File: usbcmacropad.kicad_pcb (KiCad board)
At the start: 2 copper layers, 81 x 45.2 mm, 6 parts, among them SW1 SW_Push, SW2 SW_Push, SW3 SW_Push, SW4 SW_Push, U1 XIAO-RP2040-DIP

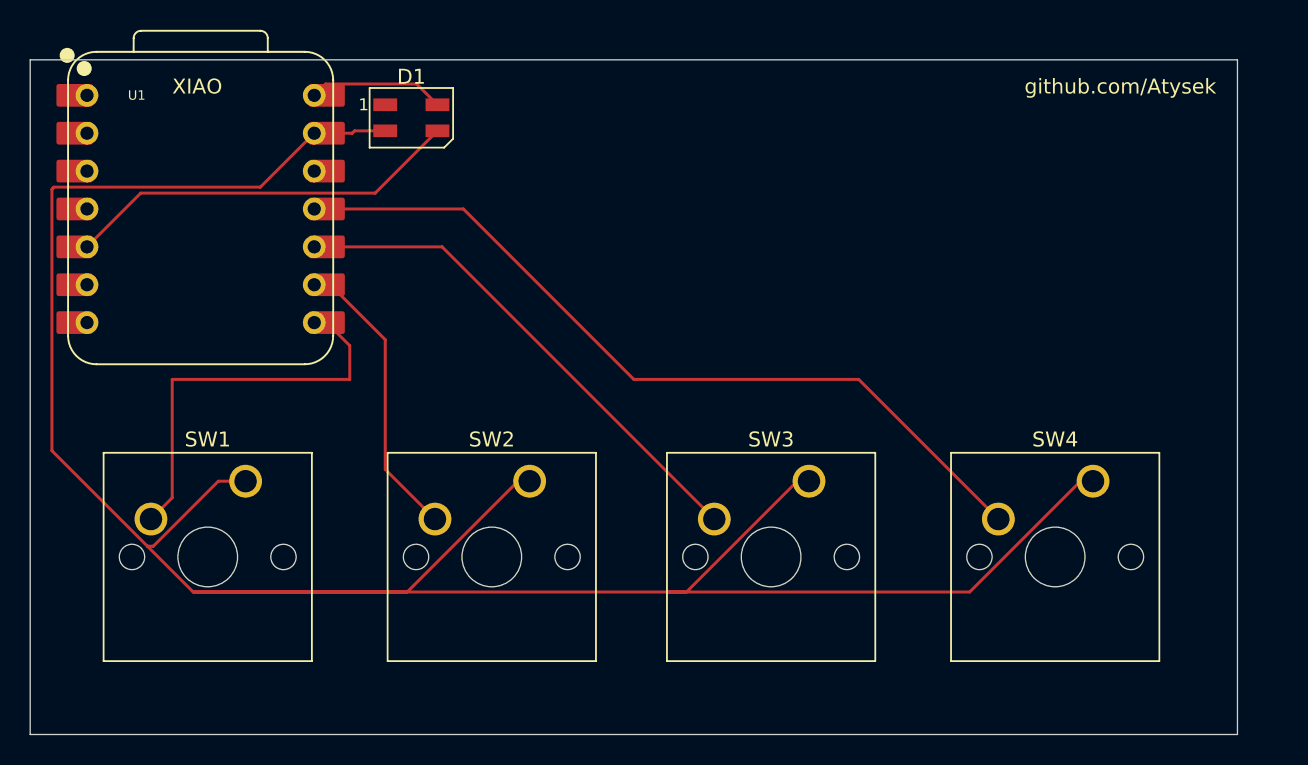
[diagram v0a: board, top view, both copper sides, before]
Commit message: Added OLED Display and edited connections
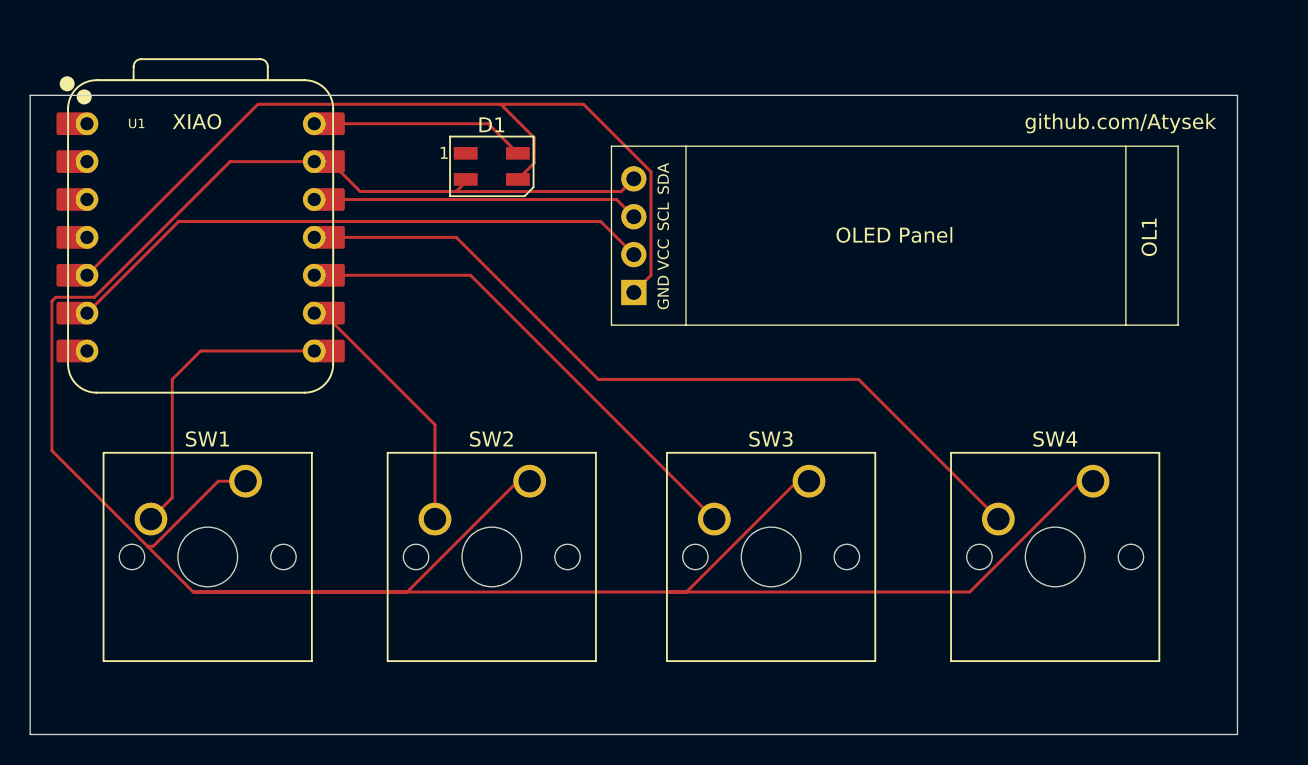
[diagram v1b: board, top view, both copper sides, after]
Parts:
- added OL1: OLED, oled:SSD1306-0.91-OLED-4pin-128x32, F.Cu at (146.0, 89.2)
- moved D1 6.30 mm to (100.0, 78.6)
- moved U1 1.91 mm to (80.5, 83.3)
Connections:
- U1 pad 12: unconnected-(U1-3V3-Pad12) -> Net-(OL1-VCC)
- U1 pad 6: unconnected-(U1-GPIO7/SCL-Pad6) -> Net-(OL1-SCL)
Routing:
- net Net-(OL1-SCL): track 0.00 -> 40.1 mm
- net Net-(D1-DIN): track 26.7 -> 60.5 mm
- net Net-(OL1-VCC): track 0.00 -> 22.8 mm
- net GND: track 164.8 -> 178.5 mm
- net Net-(U1-GPIO1/RX): track 27.1 -> 20.3 mm
- net +5V: track 9.16 -> 14.5 mm
- net Net-(U1-GPIO2/SCK): track 19.7 -> 18.4 mm
- net Net-(U1-GPIO3/MOSI): track 54.5 -> 53.7 mm
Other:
- board size 81 x 45.2 mm -> 81 x 42.9 mm
